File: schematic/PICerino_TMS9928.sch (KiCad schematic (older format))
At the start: 65 parts, among them CON1 PICERINO-EDGE, J1 Conn_01x02, J10 Conn_01x08, J11 Conn_01x08, J12 Conn_01x03, J2 Y_Conn_01x02, J3 BY_Conn_01x02, J4 RY_Conn_01x02, J5 Y_Conn_01x02, J6 Conn_01x02, J7 Conn_01x02, J8 Conn_01x02, J9 Conn_01x02, Q1 2N3904, Y1 Crystal

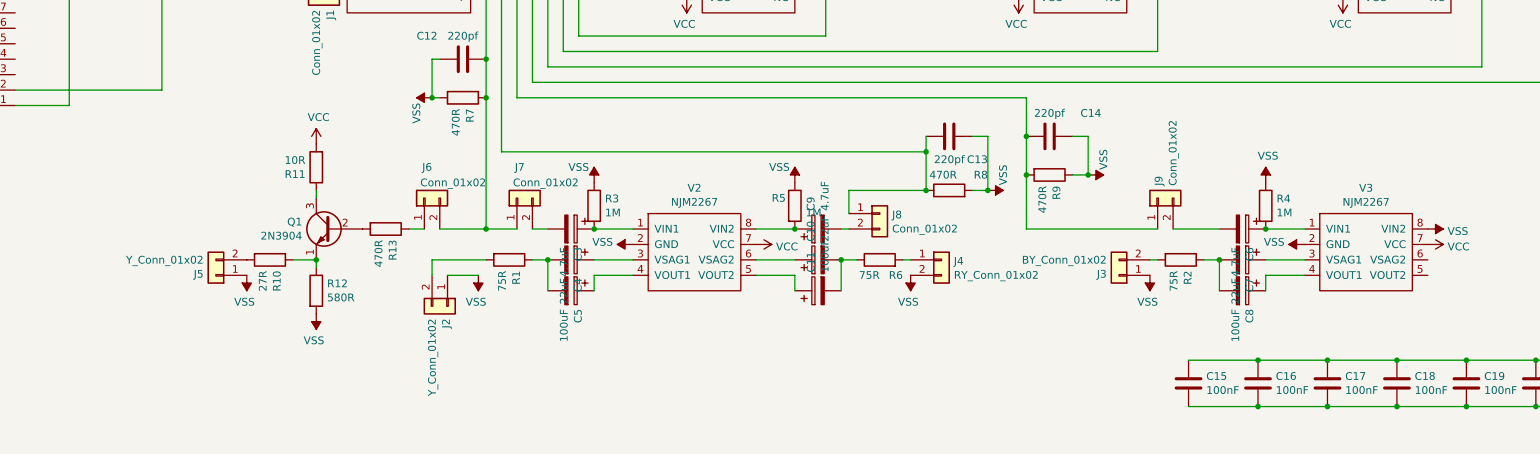
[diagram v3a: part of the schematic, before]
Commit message: removed luma circuit, no need. added 75ohm voltage divider per the 2267 data sheet. do not populate for 6db increase, other wise use it for most applications.
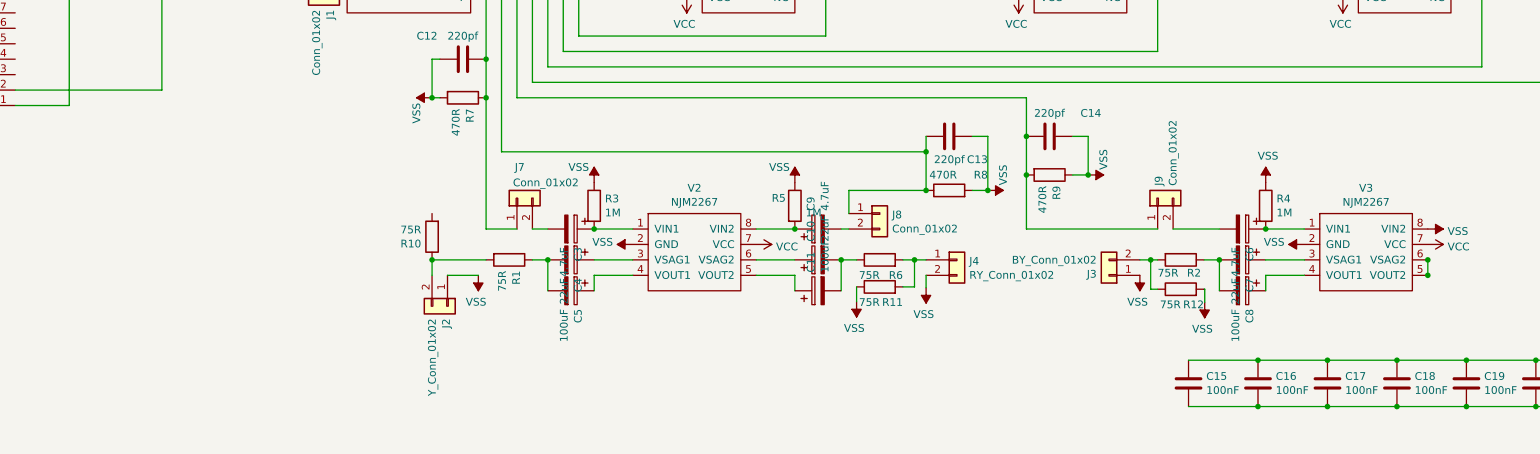
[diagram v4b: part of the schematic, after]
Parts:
- removed J5: Y_Conn_01x02, Connector_PinHeader_2.54mm:PinHeader_1x02_P2.54mm_Vertical, symbol Connector_Generic:Conn_01x02
- removed J6: Conn_01x02, Connector_PinHeader_2.54mm:PinHeader_1x02_P2.54mm_Vertical, symbol Connector_Generic:Conn_01x02
- removed Q1: 2N3904, Package_TO_SOT_THT:TO-92_Wide, symbol Transistor_BJT:2N3904
- removed R13: 470R, Resistor_THT:R_Axial_DIN0207_L6.3mm_D2.5mm_P7.62mm_Horizontal, symbol Device:R
- R10: value 27R -> 75R; footprint Resistor_THT:R_Axial_DIN0207_L6.3mm_D2.5mm_P7.62mm_Horizontal -> Resistor_THT:R_Axial_DIN0207_L6.3mm_D2.5mm_P2.54mm_Vertical
- R11: value 10R -> 75R; footprint Resistor_THT:R_Axial_DIN0207_L6.3mm_D2.5mm_P7.62mm_Horizontal -> Resistor_THT:R_Axial_DIN0207_L6.3mm_D2.5mm_P2.54mm_Vertical
- R12: value 580R -> 75R; footprint Resistor_THT:R_Axial_DIN0207_L6.3mm_D2.5mm_P7.62mm_Horizontal -> Resistor_THT:R_Axial_DIN0207_L6.3mm_D2.5mm_P2.54mm_Vertical
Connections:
- net VCC: no longer R11.2
- net VSS: now also R11.1
- net at V3.5 (VOUT2): now also V3.6 (VSAG2)
- net at J2.2 (Pin_2), R1.2: now also R10.1
- net at J4.1 (Pin_1), R6.2: now also R11.2
- net at R12.1: now also J3.2 (Pin_2), R2.2; no longer R10.1
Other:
- moved on the sheet: J3, J4
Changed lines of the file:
@@
 L Connector_Generic:Conn_01x02 J4
 U 1 1 61DE8160
-P 9200 7350
-F 0 "J4" H 9280 7342 50  0000 L CNN
-F 1 "RY_Conn_01x02" H 9280 7251 50  0000 L CNN
-F 2 "Connector_PinHeader_2.54mm:PinHeader_1x02_P2.54mm_Vertical" H 9200 7350 50  0001 C CNN
-F 3 "~" H 9200 7350 50  0001 C CNN
-	1    9200 7350
+P 9300 7350
+F 0 "J4" H 9380 7342 50  0000 L CNN
+F 1 "RY_Conn_01x02" H 9380 7251 50  0000 L CNN
+F 2 "Connector_PinHeader_2.54mm:PinHeader_1x02_P2.54mm_Vertical" H 9300 7350 50  0001 C CNN
+F 3 "~" H 9300 7350 50  0001 C CNN
+	1    9300 7350
 	1    0    0    -1
 $EndComp
@@
 U 1 1 62BF1201
 P 10750 7350
-F 0 "R2" H 10820 7396 50  0000 L CNN
-F 1 "75R" H 10820 7305 50  0000 L CNN
+F 0 "R2" V 10835 7390 50  0000 L CNN
+F 1 "75R" V 10835 7200 50  0000 L CNN
 F 2 "Resistor_THT:R_Axial_DIN0207_L6.3mm_D2.5mm_P2.54mm_Vertical" V 10680 7350 50  0001 C CNN
 F 3 "~" H 10750 7350 50  0001 C CNN
@@
 L Connector_Generic:Conn_01x02 J3
 U 1 1 62E1822F
-P 10350 7450
-F 0 "J3" H 10430 7442 50  0000 L CNN
-F 1 "BY_Conn_01x02" H 10430 7351 50  0000 L CNN
-F 2 "Connector_PinHeader_2.54mm:PinHeader_1x02_P2.54mm_Vertical" H 10350 7450 50  0001 C CNN
-F 3 "~" H 10350 7450 50  0001 C CNN
-	1    10350 7450
+P 10285 7450
+F 0 "J3" H 10365 7442 50  0000 L CNN
+F 1 "BY_Conn_01x02" H 10365 7351 50  0000 L CNN
+F 2 "Connector_PinHeader_2.54mm:PinHeader_1x02_P2.54mm_Vertical" H 10285 7450 50  0001 C CNN
+F 3 "~" H 10285 7450 50  0001 C CNN
+	1    10285 7450
 	-1   0    0    1
 $EndComp
-Wire Wire Line
-	9000 7350 8950 7350
-Wire Wire Line
-	10550 7350 10600 7350
 Wire Wire Line
 	9750 7150 10600 7150
@@
 L power:VSS #PWR0137
 U 1 1 62EA0F96
-P 10550 7450
-F 0 "#PWR0137" H 10550 7300 50  0001 C CNN
-F 1 "VSS" H 10565 7623 50  0000 C CNN
-F 2 "" H 10550 7450 50  0001 C CNN
-F 3 "" H 10550 7450 50  0001 C CNN
-	1    10550 7450
-	-1   0    0    1
-$EndComp
-$Comp
-L power:VSS #PWR0138
-U 1 1 62EA14CA
-P 9000 7450
-F 0 "#PWR0138" H 9000 7300 50  0001 C CNN
-F 1 "VSS" H 9015 7623 50  0000 C CNN
-F 2 "" H 9000 7450 50  0001 C CNN
-F 3 "" H 9000 7450 50  0001 C CNN
-	1    9000 7450
+P 10485 7450
+F 0 "#PWR0137" H 10485 7300 50  0001 C CNN
+F 1 "VSS" H 10500 7623 50  0000 C CNN
+F 2 "" H 10485 7450 50  0001 C CNN
+F 3 "" H 10485 7450 50  0001 C CNN
+	1    10485 7450
 	-1   0    0    1
 $EndComp
@@
 $EndComp
 $Comp
-L Device:R R13
-U 1 1 621EC96B
-P 5600 7150
-F 0 "R13" H 5670 7196 50  0000 L CNN
-F 1 "470R" H 5670 7105 50  0000 L CNN
-F 2 "Resistor_THT:R_Axial_DIN0207_L6.3mm_D2.5mm_P7.62mm_Horizontal" V 5530 7150 50  0001 C CNN
-F 3 "~" H 5600 7150 50  0001 C CNN
-	1    5600 7150
-	0    1    1    0
-$EndComp
-$Comp
-L Device:R R12
-U 1 1 621ED65B
-P 5150 7550
-F 0 "R12" H 5220 7596 50  0000 L CNN
-F 1 "580R" H 5220 7505 50  0000 L CNN
-F 2 "Resistor_THT:R_Axial_DIN0207_L6.3mm_D2.5mm_P7.62mm_Horizontal" V 5080 7550 50  0001 C CNN
-F 3 "~" H 5150 7550 50  0001 C CNN
-	1    5150 7550
-	1    0    0    -1
-$EndComp
-$Comp
-L Device:R R10
-U 1 1 621EDD1D
-P 4850 7350
-F 0 "R10" H 4920 7396 50  0000 L CNN
-F 1 "27R" H 4920 7305 50  0000 L CNN
-F 2 "Resistor_THT:R_Axial_DIN0207_L6.3mm_D2.5mm_P7.62mm_Horizontal" V 4780 7350 50  0001 C CNN
-F 3 "~" H 4850 7350 50  0001 C CNN
-	1    4850 7350
-	0    1    1    0
-$EndComp
-$Comp
-L Device:R R11
-U 1 1 621EE775
-P 5150 6750
-F 0 "R11" H 5220 6796 50  0000 L CNN
-F 1 "10R" H 5220 6705 50  0000 L CNN
-F 2 "Resistor_THT:R_Axial_DIN0207_L6.3mm_D2.5mm_P7.62mm_Horizontal" V 5080 6750 50  0001 C CNN
-F 3 "~" H 5150 6750 50  0001 C CNN
-	1    5150 6750
-	-1   0    0    1
-$EndComp
-$Comp
-L Transistor_BJT:2N3904 Q1
-U 1 1 621EFA7A
-P 5250 7150
-F 0 "Q1" H 5441 7196 50  0000 L CNN
-F 1 "2N3904" H 5441 7105 50  0000 L CNN
-F 2 "Package_TO_SOT_THT:TO-92_Wide" H 5450 7075 50  0001 L CIN
-F 3 "https://www.onsemi.com/pub/Collateral/2N3903-D.PDF" H 5250 7150 50  0001 L CNN
-	1    5250 7150
-	-1   0    0    -1
-$EndComp
-$Comp
 L Device:C C12
 U 1 1 622305A4
@@
 	5900 6300 5950 6300
 Connection ~ 5900 6300
-$Comp
-L Connector_Generic:Conn_01x02 J5
-U 1 1 623A35B7
-P 4500 7450
-F 0 "J5" H 4580 7442 50  0000 L CNN
-F 1 "Y_Conn_01x02" H 4580 7351 50  0000 L CNN
-F 2 "Connector_PinHeader_2.54mm:PinHeader_1x02_P2.54mm_Vertical" H 4500 7450 50  0001 C CNN
-F 3 "~" H 4500 7450 50  0001 C CNN
-	1    4500 7450
-	-1   0    0    1
-$EndComp
-Wire Wire Line
-	5000 7350 5150 7350
-Wire Wire Line
-	5150 7350 5150 7400
-Connection ~ 5150 7350
-$Comp
-L power:VSS #PWR0148
-U 1 1 624009C6
-P 4700 7450
-F 0 "#PWR0148" H 4700 7300 50  0001 C CNN
-F 1 "VSS" H 4715 7623 50  0000 C CNN
-F 2 "" H 4700 7450 50  0001 C CNN
-F 3 "" H 4700 7450 50  0001 C CNN
-	1    4700 7450
-	-1   0    0    1
-$EndComp
-$Comp
-L power:VSS #PWR0149
-U 1 1 6240248C
-P 5150 7700
-F 0 "#PWR0149" H 5150 7550 50  0001 C CNN
-F 1 "VSS" H 5165 7873 50  0000 C CNN
-F 2 "" H 5150 7700 50  0001 C CNN
-F 3 "" H 5150 7700 50  0001 C CNN
-	1    5150 7700
-	-1   0    0    1
-$EndComp
 Wire Wire Line
 	5900 7450 5900 7350
@@
 Wire Wire Line
 	6200 7450 6000 7450
-Wire Wire Line
-	5150 6950 5150 6900
 Wire Wire Line
 	9500 6900 9400 6900
@@
 	9500 6550 9400 6550
 Connection ~ 9500 6900
-$Comp
-L power:VCC #PWR0150
-U 1 1 624F8511
-P 5150 6600
-F 0 "#PWR0150" H 5150 6450 50  0001 C CNN
-F 1 "VCC" H 5165 6773 50  0000 C CNN
-F 2 "" H 5150 6600 50  0001 C CNN
-F 3 "" H 5150 6600 50  0001 C CNN
-	1    5150 6600
-	1    0    0    -1
-$EndComp
 $Comp
 L Device:C_Variable C26
@@
 Wire Wire Line
 	4500 5050 4550 5050
-$Comp
-L Connector_Generic:Conn_01x02 J6
-U 1 1 6232D5AF
-P 5850 6950
-F 0 "J6" V 6050 6900 50  0000 L CNN
-F 1 "Conn_01x02" V 5950 6550 50  0000 L CNN
-F 2 "Connector_PinHeader_2.54mm:PinHeader_1x02_P2.54mm_Vertical" H 5850 6950 50  0001 C CNN
-F 3 "~" H 5850 6950 50  0001 C CNN
-	1    5850 6950
-	0    -1   -1   0
-$EndComp
 Connection ~ 6250 6300
 $Comp
@@
 RnW
 Wire Wire Line
-	5750 7150 5850 7150
-Wire Wire Line
 	7450 3950 9000 3950
 Wire Wire Line
@@
 	6250 3550 8600 3550
 Wire Wire Line
-	5950 7150 6250 7150
-Wire Wire Line
 	6250 6300 6250 7150
-Connection ~ 6250 7150
 Wire Wire Line
 	6250 7150 6450 7150
+$Comp
+L Device:R R10
+U 1 1 625FCCF9
+P 5900 7200
+F 0 "R10" H 5970 7246 50  0000 L CNN
+F 1 "75R" H 5970 7155 50  0000 L CNN
+F 2 "Resistor_THT:R_Axial_DIN0207_L6.3mm_D2.5mm_P2.54mm_Vertical" V 5830 7200 50  0001 C CNN
+F 3 "~" H 5900 7200 50  0001 C CNN
+	1    5900 7200
+	-1   0    0    1
+$EndComp
+Connection ~ 5900 7350
+$Comp
+L Device:R R11
+U 1 1 625FE7A4
+P 8800 7525
+F 0 "R11" V 8700 7375 50  0000 L CNN
+F 1 "75R" V 8700 7525 50  0000 L CNN
+F 2 "Resistor_THT:R_Axial_DIN0207_L6.3mm_D2.5mm_P2.54mm_Vertical" V 8730 7525 50  0001 C CNN
+F 3 "~" H 8800 7525 50  0001 C CNN
+	1    8800 7525
+	0    -1   -1   0
+$EndComp
+$Comp
+L power:VSS #PWR02
+U 1 1 6264401E
+P 9100 7530
+F 0 "#PWR02" H 9100 7380 50  0001 C CNN
+F 1 "VSS" H 9115 7703 50  0000 C CNN
+F 2 "" H 9100 7530 50  0001 C CNN
+F 3 "" H 9100 7530 50  0001 C CNN
+	1    9100 7530
+	-1   0    0    1
+$EndComp
+Wire Wire Line
+	9100 7530 9100 7450
+Wire Wire Line
+	8950 7350 9025 7350
+Wire Wire Line
+	8950 7525 9025 7525
+Wire Wire Line
+	9025 7525 9025 7350
+Connection ~ 9025 7350
+Wire Wire Line
+	9025 7350 9100 7350
+$Comp
+L power:VSS #PWR01
+U 1 1 626D8E8A
+P 8650 7620
+F 0 "#PWR01" H 8650 7470 50  0001 C CNN
+F 1 "VSS" H 8665 7793 50  0000 C CNN
+F 2 "" H 8650 7620 50  0001 C CNN
+F 3 "" H 8650 7620 50  0001 C CNN
+	1    8650 7620
+	-1   0    0    1
+$EndComp
+Wire Wire Line
+	8650 7620 8650 7525
+$Comp
+L Device:R R12
+U 1 1 62745639
+P 10750 7540
+F 0 "R12" V 10650 7390 50  0000 L CNN
+F 1 "75R" V 10650 7540 50  0000 L CNN
+F 2 "Resistor_THT:R_Axial_DIN0207_L6.3mm_D2.5mm_P2.54mm_Vertical" V 10680 7540 50  0001 C CNN
+F 3 "~" H 10750 7540 50  0001 C CNN
+	1    10750 7540
+	0    -1   -1   0
+$EndComp
+Wire Wire Line
+	10600 7540 10555 7540
+Wire Wire Line
+	10555 7540 10555 7350
+Wire Wire Line
+	10485 7350 10555 7350
+Connection ~ 10555 7350
+Wire Wire Line
+	10555 7350 10600 7350
+$Comp
+L power:VSS #PWR03
+U 1 1 6277B254
+P 10905 7625
+F 0 "#PWR03" H 10905 7475 50  0001 C CNN
+F 1 "VSS" H 10920 7798 50  0000 C CNN
+F 2 "" H 10905 7625 50  0001 C CNN
+F 3 "" H 10905 7625 50  0001 C CNN
+	1    10905 7625
+	-1   0    0    1
+$EndComp
+Wire Wire Line
+	10905 7540 10900 7540
+Wire Wire Line
+	10905 7540 10905 7625
+Wire Wire Line
+	12350 7345 12350 7350
+Wire Wire Line
+	12350 7450 12345 7450
 Wire Bus Line
 	5000 3550 5000 4250
 Wire Bus Line
 	3500 3550 3500 4250
+Connection ~ 12350 7450
+Connection ~ 12350 7350
+Wire Wire Line
+	12350 7350 12350 7450
 $EndSCHEMATC

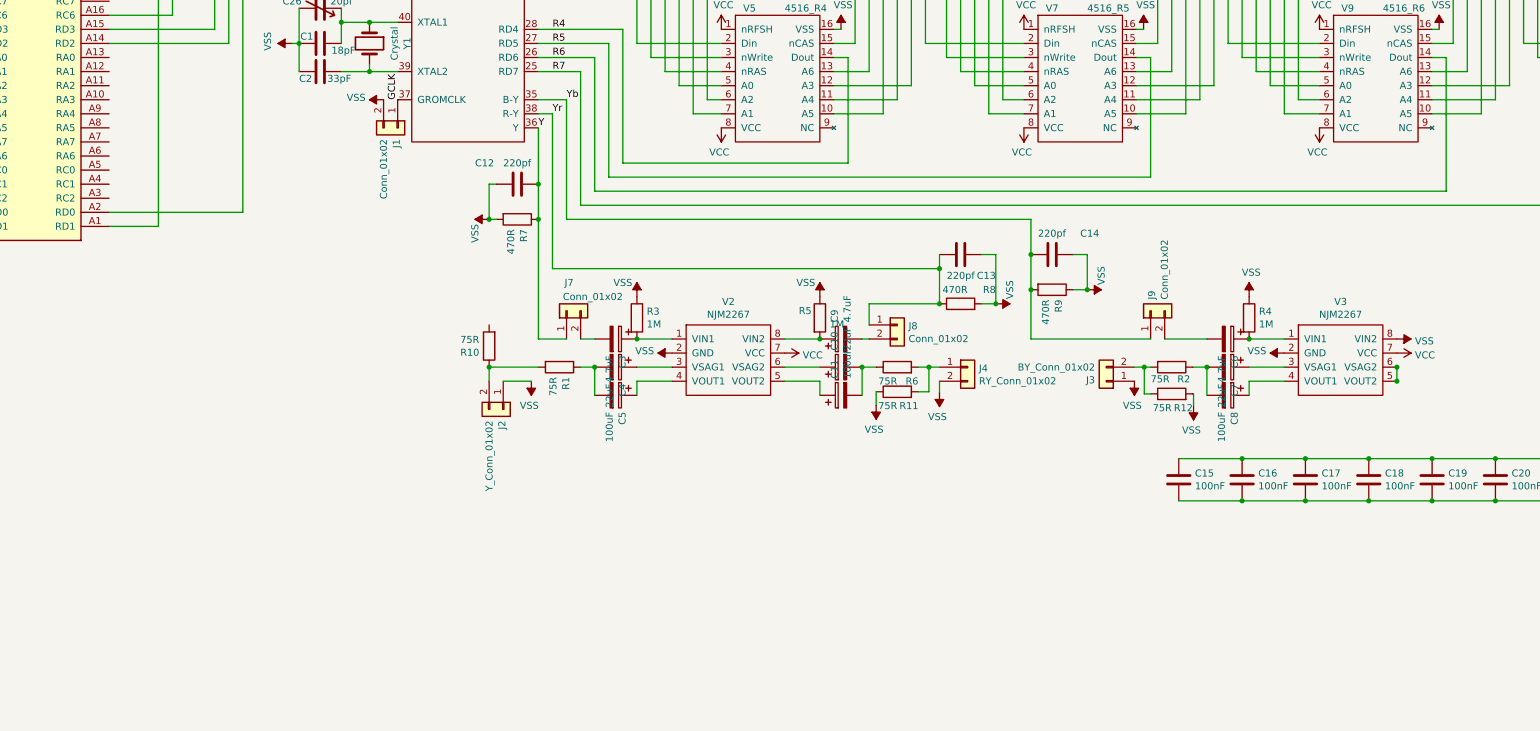
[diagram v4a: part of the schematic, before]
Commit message: updated schematic of TMS9928. This will work for 9918, and 9929 as well. Only Y is needed for 9918, and 9929 requires a different crystal. One item to point out is this video circuit is only supposed to be a buffer AC output. This isn't correct for Y on the component video. It does work with the retrotink-2x and gefen component to hdmi converters. haven't tested for a strong blue issue yet, doesn't seem to do that. Also jumpers are inserted on the board to bring out TMS99XX video signals out to whatever video circuit is desired
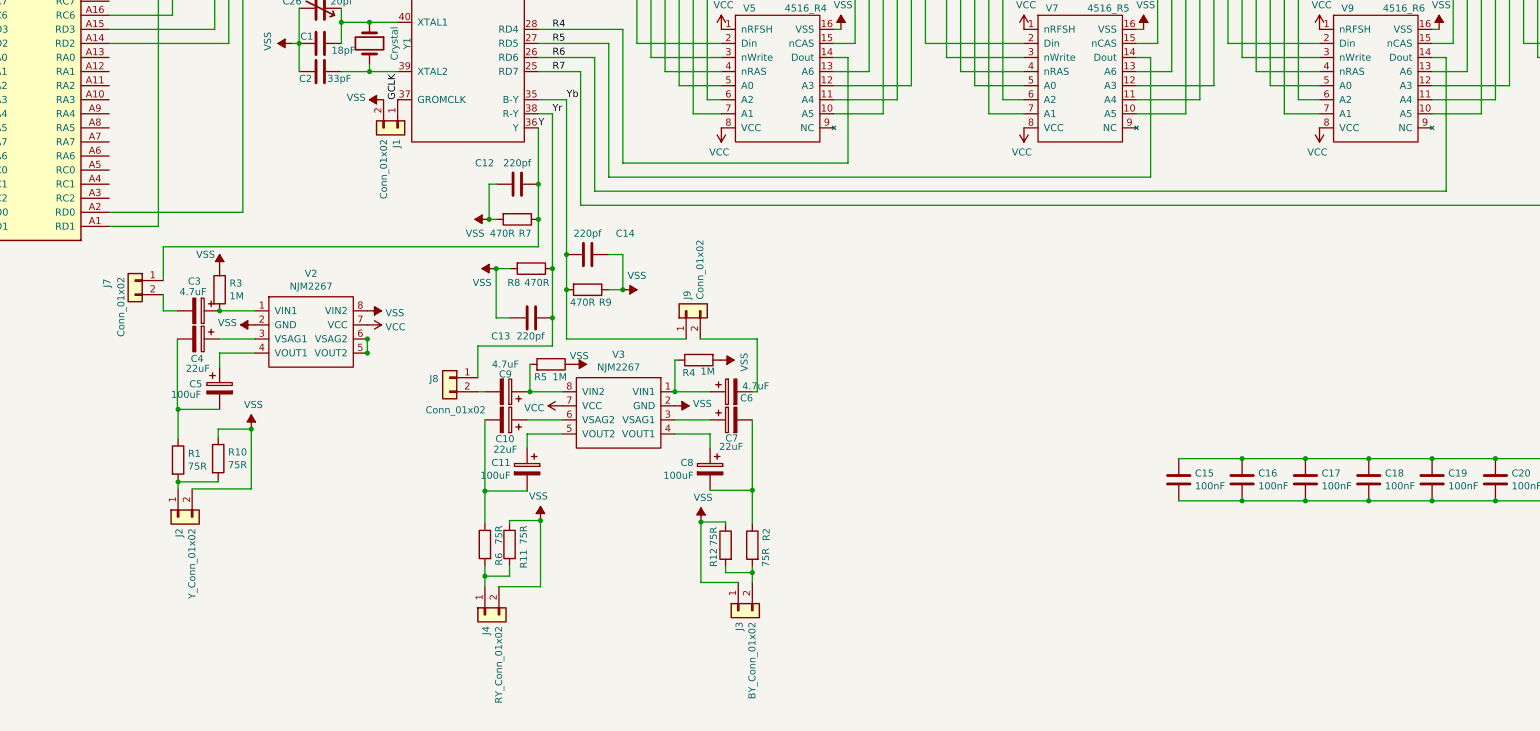
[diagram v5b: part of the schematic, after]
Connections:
- net VSS: now also J2.2 (Pin_2), R10.1, R12.1, R4.2, V2.8 (VIN2); no longer J2.1 (Pin_1), R12.2, R4.1, V3.8 (VIN2)
- net at C6.1, V3.1 (VIN1): now also R4.1; no longer R4.2
- net at V3.5 (VOUT2): now also C11.1; no longer V3.6 (VSAG2)
- net at V2.5 (VOUT2): now also V2.6 (VSAG2); no longer C11.1
- net at C10.1: now also V3.6 (VSAG2); no longer V2.6 (VSAG2)
- net at C9.1, R5.2: now also V3.8 (VIN2); no longer V2.8 (VIN2)
- net at R10.2: now also J2.1 (Pin_1), R1.2
- net at J3.2 (Pin_2), R2.2: now also R12.2; no longer R12.1
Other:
- moved on the sheet: C10, C11, C13, C14, C3, C4, C5, C6, C7, C8, C9, J2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
